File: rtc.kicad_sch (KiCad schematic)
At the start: 7 parts, among them U6 DS3231MZ

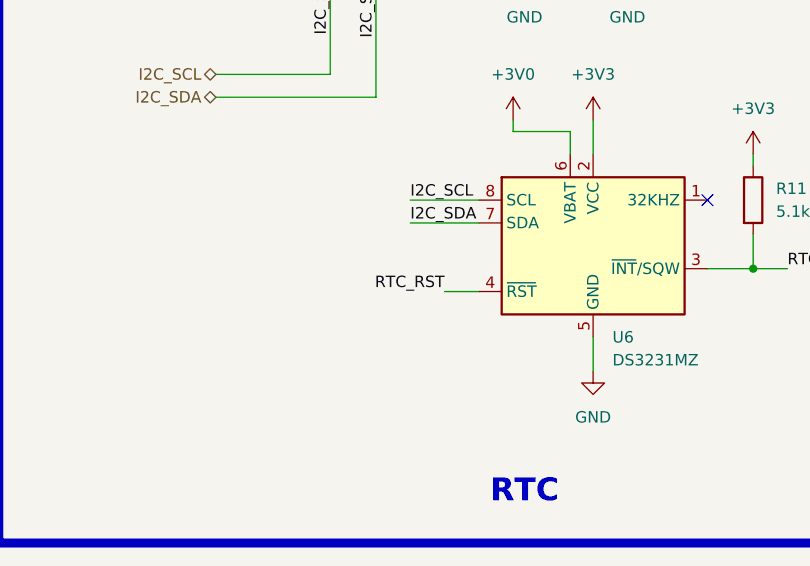
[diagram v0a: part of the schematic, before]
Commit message: Retry with rules DRC ERC passing
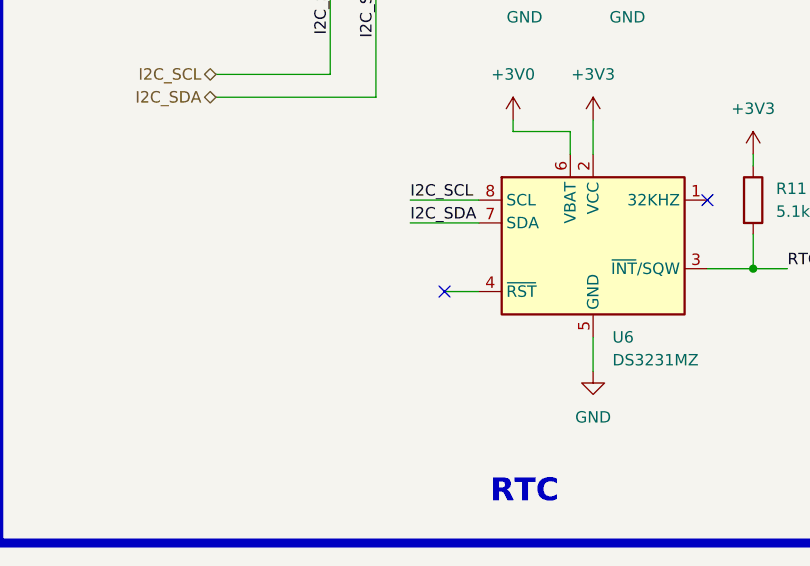
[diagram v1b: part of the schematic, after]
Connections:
- net RTC_RST: no longer names the net of U6.4 (~{RST})
- no-connect marks 1 -> 2
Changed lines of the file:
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@@
 		(at 166.37 92.71)
+	)
+	(no_connect
+		(at 137.16 102.87)
 	)
 	(wire
@@
 		)
 	)
-	(label "RTC_RST"
-		(at 137.16 102.87 180)
-		(effects
-			(font
-				(size 1.27 1.27)
-			)
-			(justify right bottom)
-		)
-	)
